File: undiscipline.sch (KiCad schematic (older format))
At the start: 177 parts, among them J1 Conn_01x04_Male, J2 USB_B_Micro, J3 Conn_01x02_Male, J4 Conn_01x02_Male, SW1 SW_Push, SW10 SW_Push, SW11 SW_Push, SW12 SW_Push, SW13 SW_Push, SW14 SW_Push, SW15 SW_Push, SW16 SW_Push, SW17 SW_Push, SW18 SW_Push, SW19 SW_Push, SW2 SW_Push, SW20 SW_Push, SW21 SW_Push, SW22 SW_Push, SW23 SW_Push, SW24 SW_Push, SW25 SW_Push, SW26 SW_Push, SW27 SW_Push, SW28 SW_Push, SW29 SW_Push, SW3 SW_Push, SW30 SW_Push, SW31 SW_Push, SW32 SW_Push, SW33 SW_Push, SW34 SW_Push, SW35 SW_Push, SW36 SW_Push, SW37 SW_Push, SW38 SW_Push, SW39 SW_Push, SW4 SW_Push, SW40 SW_Push, SW41 SW_Push, SW42 SW_Push, SW43 SW_Push, SW44 SW_Push, SW45 SW_Push, SW46 SW_Push, SW47 SW_Push, SW48 SW_Push, SW49 SW_Push, SW5 SW_Push, SW50 SW_Push, SW51 SW_Push, SW52 SW_Push, SW53 SW_Push, SW54 SW_Push, SW55 SW_Push, SW56 SW_Push, SW57 SW_Push, SW58 SW_Push, SW59 SW_Push, SW6 SW_Push, SW60 SW_Push, SW61 SW_Push, SW62 SW_Push, SW63 SW_Push, SW64 SW_Push, SW65 SW_Push, SW66 SW_Push, SW67 SW_Push, SW68 SW_Push, SW69 SW_Push, SW7 SW_Push, SW70 SW_Push, SW71 SW_Push, SW72 SW_Push, SW73 SW_Push, SW74 SW_Push, SW75 SW_Push, SW8 SW_Push, SW9 SW_Push, U1 ATmega32A-PU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

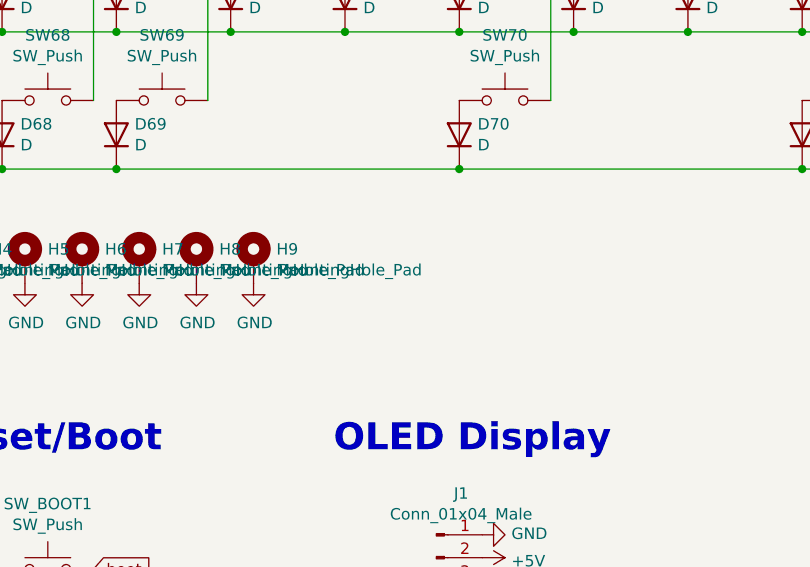
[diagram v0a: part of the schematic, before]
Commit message: Change a mounting hole
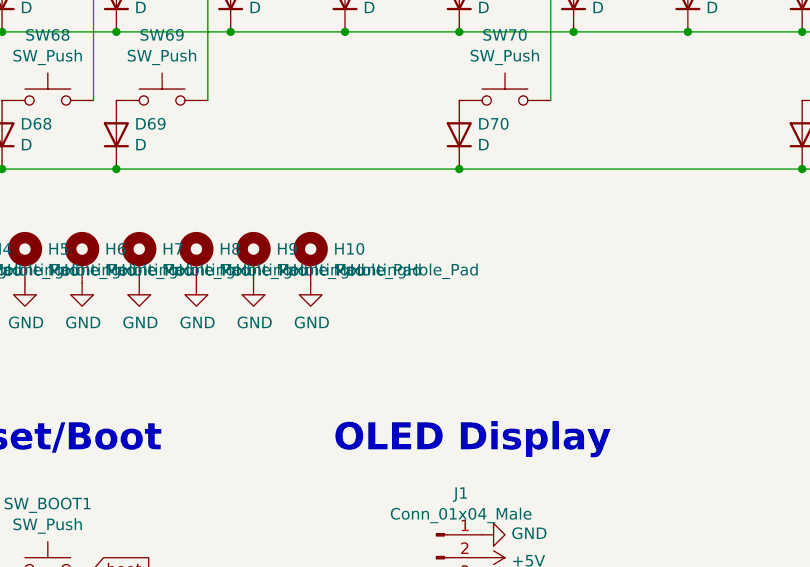
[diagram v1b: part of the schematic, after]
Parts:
- added H10: MountingHole_Pad, MountingHole:MountingHole_2.2mm_M2_DIN965_Pad_TopBottom, symbol Mechanical:MountingHole_Pad
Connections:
- net GND: now also H10.1
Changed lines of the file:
@@
 encoding utf-8
 Sheet 1 2
-Title ""
-Date ""
+Title "Undiscipline Keyboard"
+Date "2021-01-14"
 Rev ""
-Comp ""
+Comp "ILR"
 Comment1 ""
 Comment2 ""
@@
 Text GLabel 3100 1150 0    50   Input ~ 0
 row0
+$Comp
+L Mechanical:MountingHole_Pad H10
+U 1 1 600121D8
+P 5950 4550
+F 0 "H10" H 6050 4599 50  0000 L CNN
+F 1 "MountingHole_Pad" H 6050 4508 50  0000 L CNN
+F 2 "MountingHole:MountingHole_2.2mm_M2_DIN965_Pad_TopBottom" H 5950 4550 50  0001 C CNN
+F 3 "~" H 5950 4550 50  0001 C CNN
+	1    5950 4550
+	1    0    0    -1
+$EndComp
+$Comp
+L power:GND #PWR0101
+U 1 1 6001D0AA
+P 5950 4650
+F 0 "#PWR0101" H 5950 4400 50  0001 C CNN
+F 1 "GND" H 5955 4477 50  0000 C CNN
+F 2 "" H 5950 4650 50  0001 C CNN
+F 3 "" H 5950 4650 50  0001 C CNN
+	1    5950 4650
+	1    0    0    -1
+$EndComp
 $EndSCHEMATC

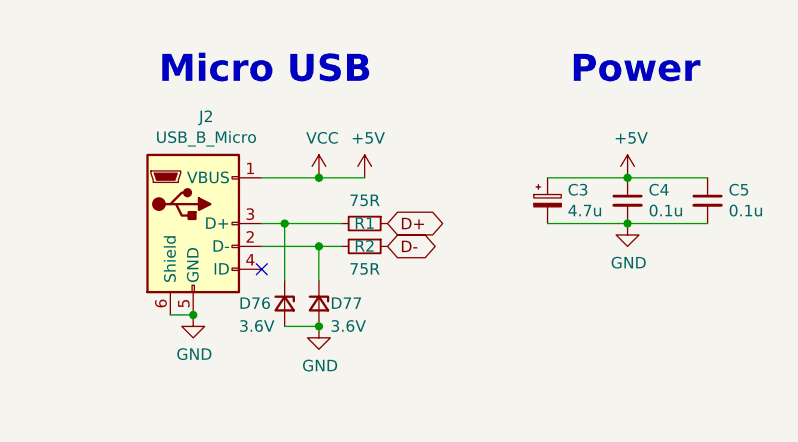
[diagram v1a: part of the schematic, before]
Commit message: Add pullup resistor to D-
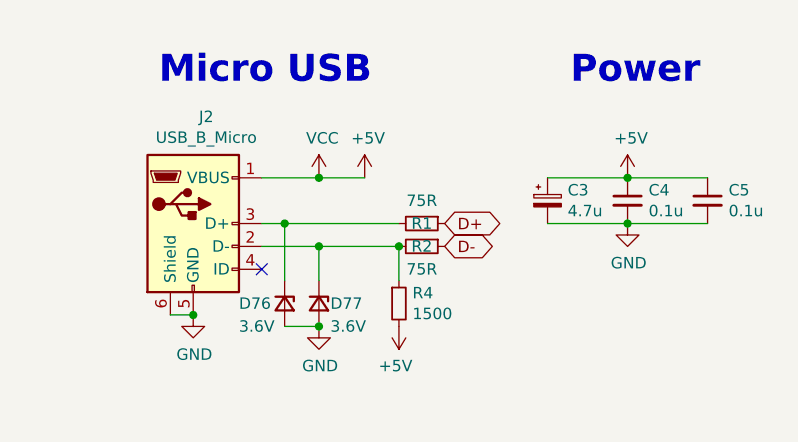
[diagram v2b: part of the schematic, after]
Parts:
- added R4: 1500, Resistor_THT:R_Axial_DIN0204_L3.6mm_D1.6mm_P5.08mm_Horizontal, symbol Device:R_Small
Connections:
- net +5V: now also R4.2
- net at D77.1 (K), J2.2 (D-), R2.2: now also R4.1
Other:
- moved on the sheet: R1, R2
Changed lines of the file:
@@
 	1    0    0    -1
 $EndComp
-Text GLabel 2100 6000 2    50   BiDi ~ 0
+Text GLabel 2350 6000 2    50   BiDi ~ 0
 D+
-Text GLabel 2100 6100 2    50   BiDi ~ 0
+Text GLabel 2350 6100 2    50   BiDi ~ 0
 D-
 NoConn ~ 1550 6200
@@
 L Device:R_Small R1
 U 1 1 600A4A74
-P 2000 6000
-F 0 "R1" V 2000 6000 50  0000 C CNN
-F 1 "75R" V 1900 6000 50  0000 C CNN
-F 2 "Resistor_THT:R_Axial_DIN0204_L3.6mm_D1.6mm_P5.08mm_Horizontal" H 2000 6000 50  0001 C CNN
-F 3 "~" H 2000 6000 50  0001 C CNN
-	1    2000 6000
+P 2250 6000
+F 0 "R1" V 2250 6000 50  0000 C CNN
+F 1 "75R" V 2150 6000 50  0000 C CNN
+F 2 "Resistor_THT:R_Axial_DIN0204_L3.6mm_D1.6mm_P5.08mm_Horizontal" H 2250 6000 50  0001 C CNN
+F 3 "~" H 2250 6000 50  0001 C CNN
+	1    2250 6000
 	0    1    1    0
 $EndComp
@@
 L Device:R_Small R2
 U 1 1 600B99AC
-P 2000 6100
-F 0 "R2" V 2000 6100 50  0000 C CNN
-F 1 "75R" V 2100 6100 50  0000 C CNN
-F 2 "Resistor_THT:R_Axial_DIN0204_L3.6mm_D1.6mm_P5.08mm_Horizontal" H 2000 6100 50  0001 C CNN
-F 3 "~" H 2000 6100 50  0001 C CNN
-	1    2000 6100
+P 2250 6100
+F 0 "R2" V 2250 6100 50  0000 C CNN
+F 1 "75R" V 2350 6100 50  0000 C CNN
+F 2 "Resistor_THT:R_Axial_DIN0204_L3.6mm_D1.6mm_P5.08mm_Horizontal" H 2250 6100 50  0001 C CNN
+F 3 "~" H 2250 6100 50  0001 C CNN
+	1    2250 6100
 	0    1    1    0
 $EndComp
@@
 Connection ~ 1800 6450
 Wire Wire Line
-	1900 6100 1800 6100
+	2150 6100 1800 6100
 Wire Wire Line
 	1800 6100 1800 6250
 Wire Wire Line
-	1900 6000 1650 6000
+	2150 6000 1650 6000
 Wire Wire Line
 	1650 6000 1650 6250
@@
 	1    0    0    -1
 $EndComp
+$Comp
+L Device:R_Small R4
+U 1 1 6004A4D2
+P 2150 6350
+F 0 "R4" H 2209 6396 50  0000 L CNN
+F 1 "1500" H 2209 6305 50  0000 L CNN
+F 2 "Resistor_THT:R_Axial_DIN0204_L3.6mm_D1.6mm_P5.08mm_Horizontal" H 2150 6350 50  0001 C CNN
+F 3 "~" H 2150 6350 50  0001 C CNN
+	1    2150 6350
+	1    0    0    -1
+$EndComp
+Wire Wire Line
+	2150 6250 2150 6100
+Connection ~ 2150 6100
+$Comp
+L power:+5V #PWR0102
+U 1 1 60083CF2
+P 2150 6450
+F 0 "#PWR0102" H 2150 6300 50  0001 C CNN
+F 1 "+5V" H 2165 6623 50  0000 C CNN
+F 2 "" H 2150 6450 50  0001 C CNN
+F 3 "" H 2150 6450 50  0001 C CNN
+	1    2150 6450
+	-1   0    0    1
+$EndComp
 $EndSCHEMATC
